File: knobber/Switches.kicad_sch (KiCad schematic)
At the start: 83 parts, among them U701 SN74LV1T34DBV

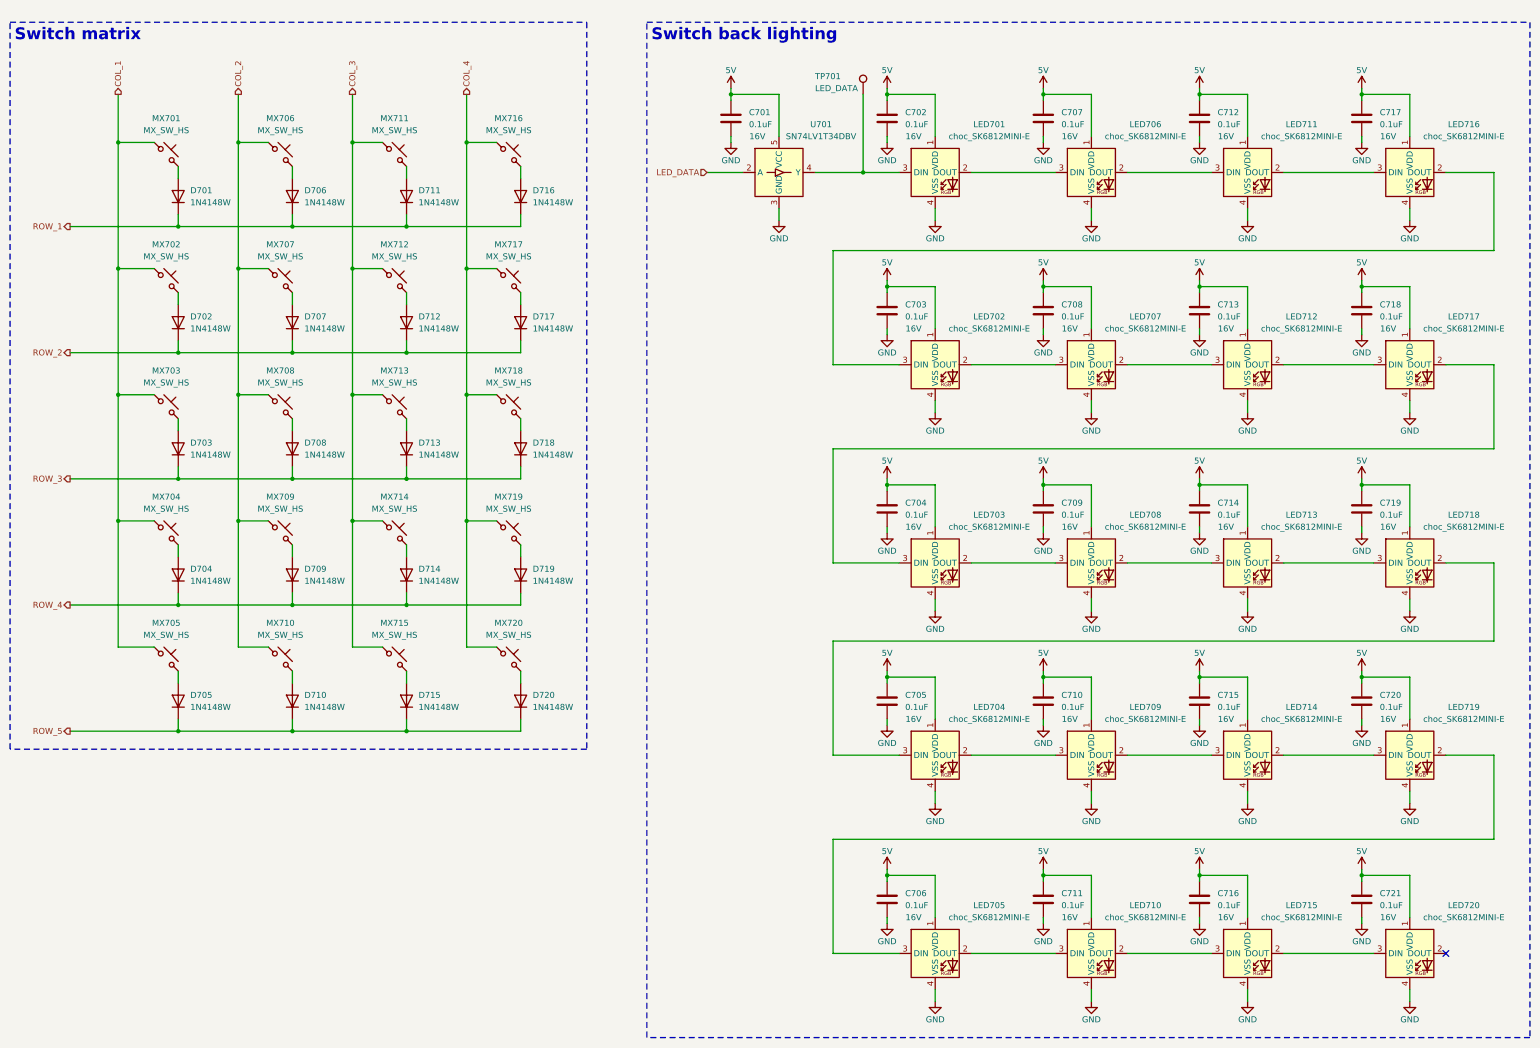
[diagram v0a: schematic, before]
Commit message: Updated schematic and PCB
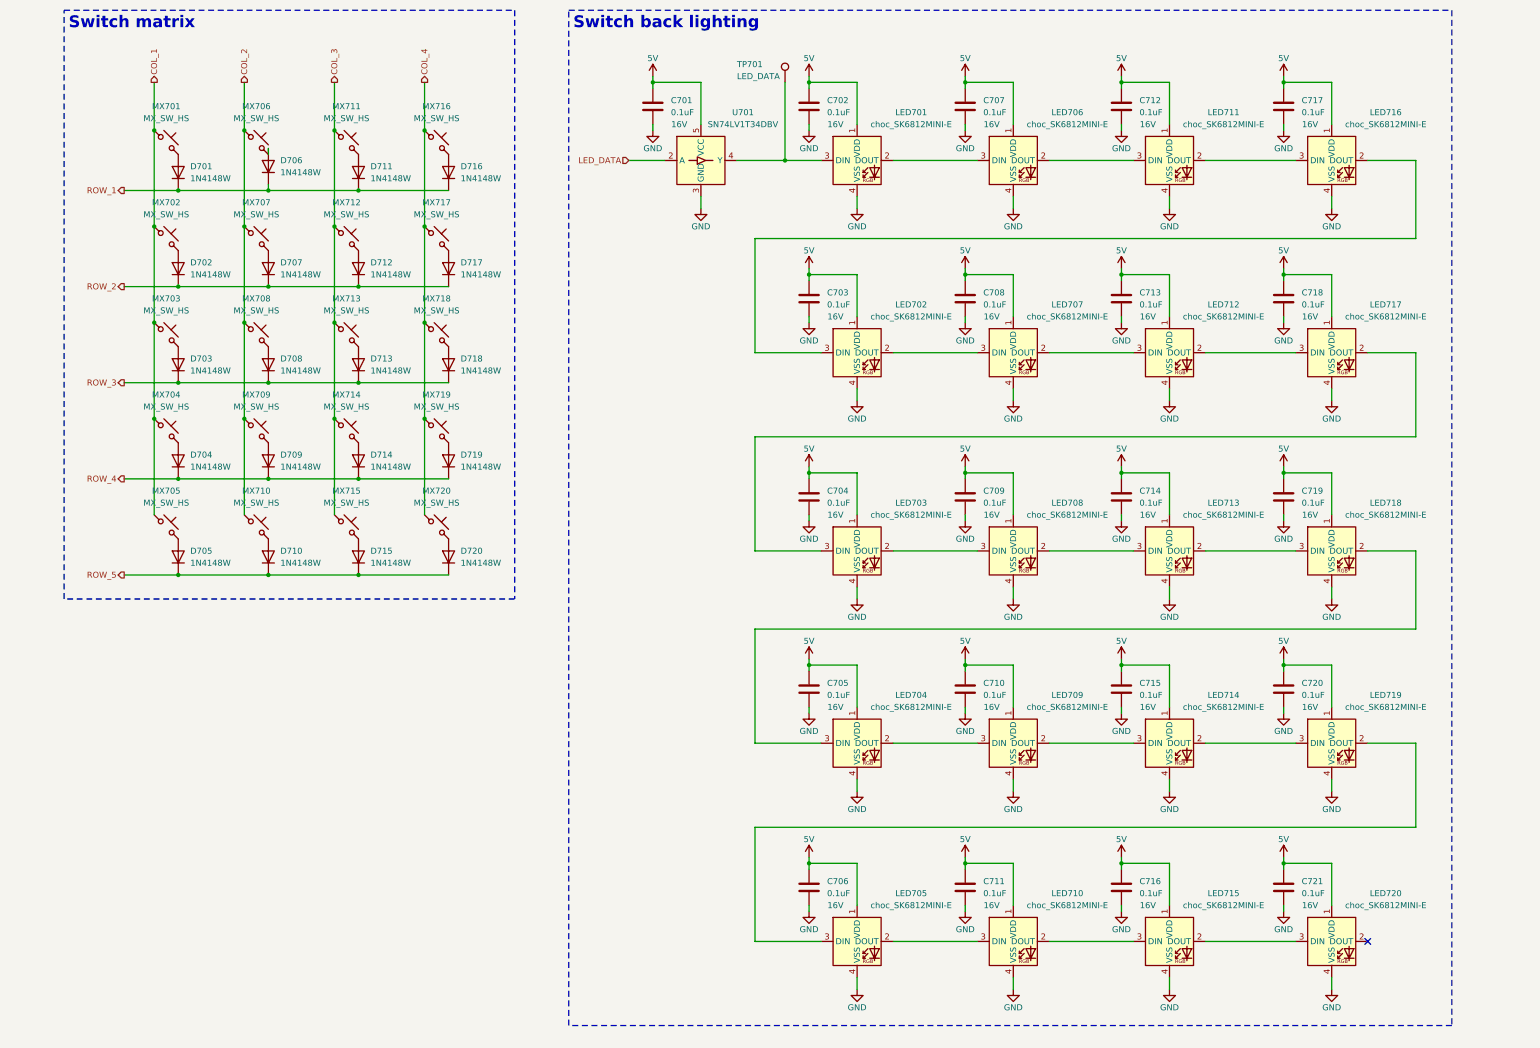
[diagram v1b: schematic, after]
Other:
- moved on the sheet: C701, C702, C703, C704, C705, C706, C707, C708, C709, C710, C711, C712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
